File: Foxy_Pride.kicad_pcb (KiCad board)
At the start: 2 copper layers, 89.3 x 67.9 mm, 36 parts, among them U1 TLC555CDR, U2 74HC4017D

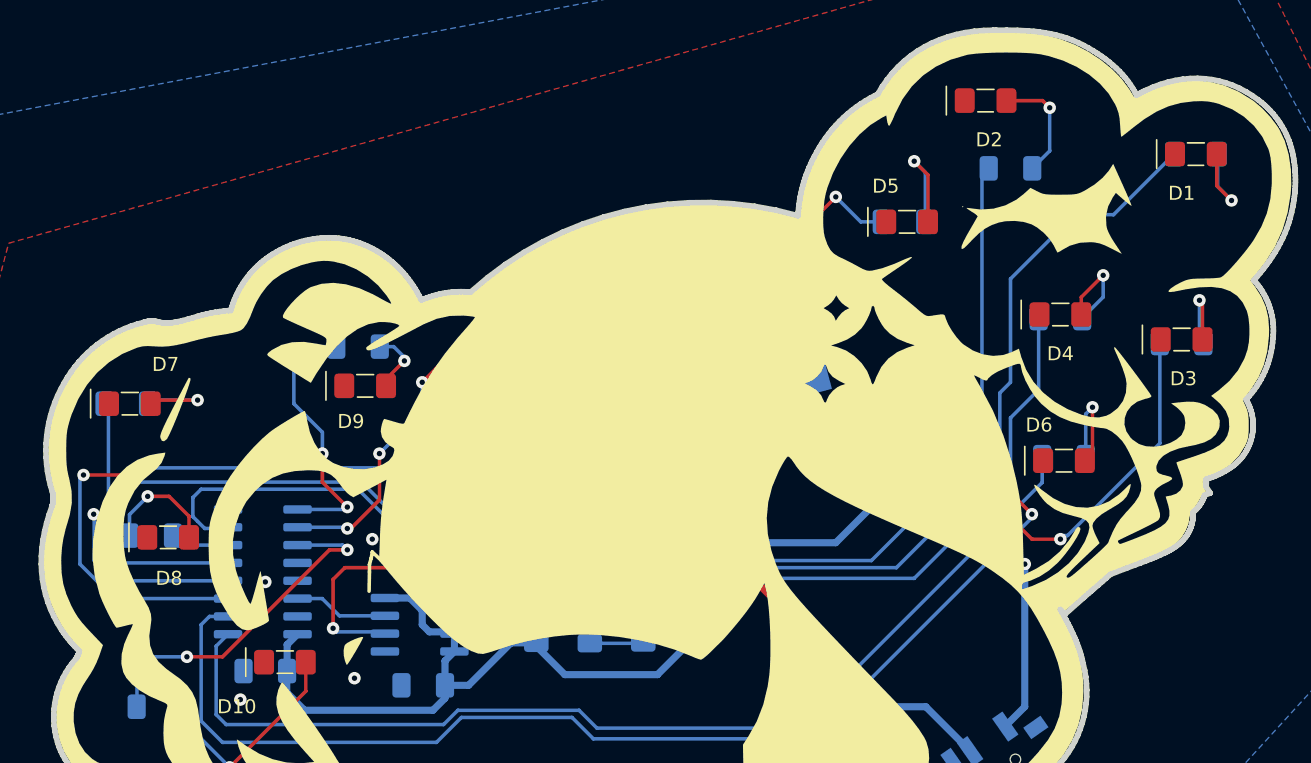
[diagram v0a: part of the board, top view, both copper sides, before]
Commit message: Re annontated schematic so resistors and LEDs have matching refrence designators
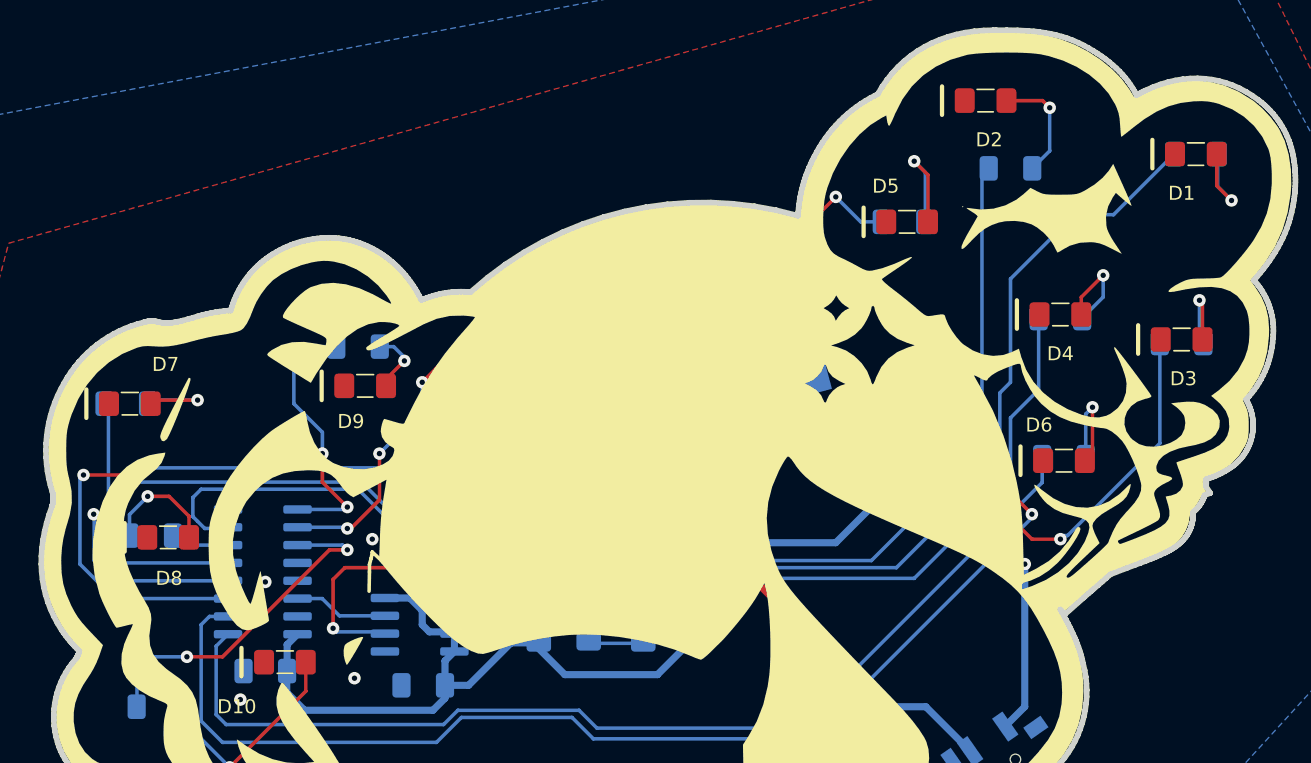
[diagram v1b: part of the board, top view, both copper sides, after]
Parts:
- removed the R1 at (61.7, 76.7)
- removed the R2 at (65.5, 76.7)
- added R11: 10M, Resistor_SMD:R_1206_3216Metric_Pad1.30x1.75mm_HandSolder, B.Cu at (61.9, 76.7)
- added R12: 2.2M, Resistor_SMD:R_1206_3216Metric_Pad1.30x1.75mm_HandSolder, B.Cu at (65.5, 76.6)
- moved G*** 2.06 mm to (85.8, 74.0)
- renumbered R3 to R1, R12 to R10, R4 to R2, R5 to R3, R6 to R4, R7 to R5, R8 to R6, R9 to R7, R10 to R8, R11 to R9
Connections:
- net +Vbatt renamed <NO NET>
- S1 pad : GND -> (no net)

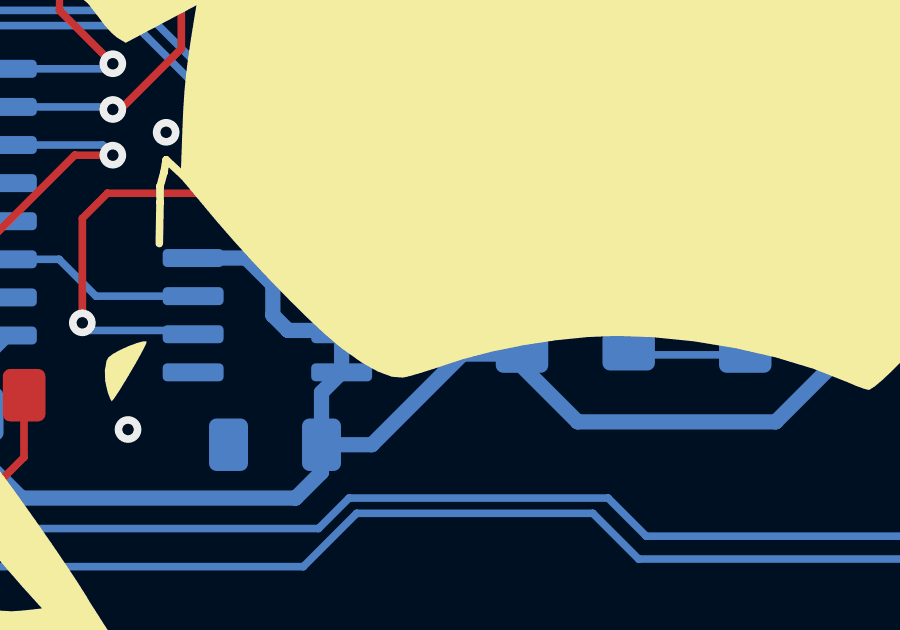
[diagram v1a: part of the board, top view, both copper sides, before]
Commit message: Changed schematic layout. Put resistor in correct spot. Update PCB.
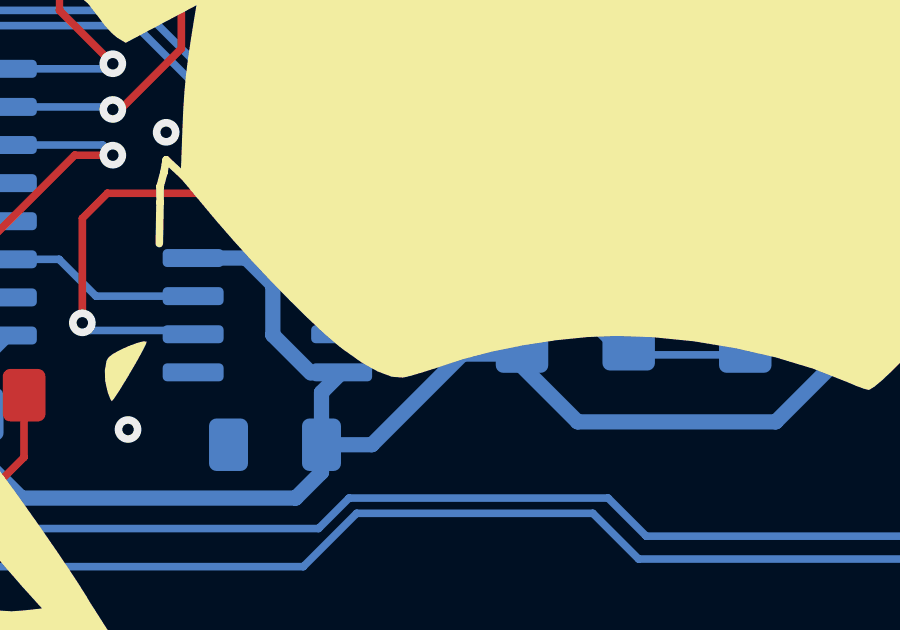
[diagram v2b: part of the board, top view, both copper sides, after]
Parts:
- renumbered G*** to ?
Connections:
- R11 pad 2: Net-(U1-Pad2) -> Net-(R11-Pad2)
- R12 pad 1: Net-(U1-Pad2) -> Net-(R11-Pad2)
- U1 pad 2: Net-(U1-Pad2) -> Net-(C1-Pad1)
- U1 pad 6: Net-(U1-Pad2) -> Net-(C1-Pad1)
- U1 pad 7: +3V -> Net-(R11-Pad2)
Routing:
- net Net-(C1-Pad1): track 3.83 -> 35.1 mm, vias 0 -> 4
- net Net-(U1-Pad2): track 30.2 -> 0.00 mm, vias 2 -> 0
- net Net-(R11-Pad2): track 0.00 -> 10.6 mm
- net +3V: track 77.0 -> 75.7 mm

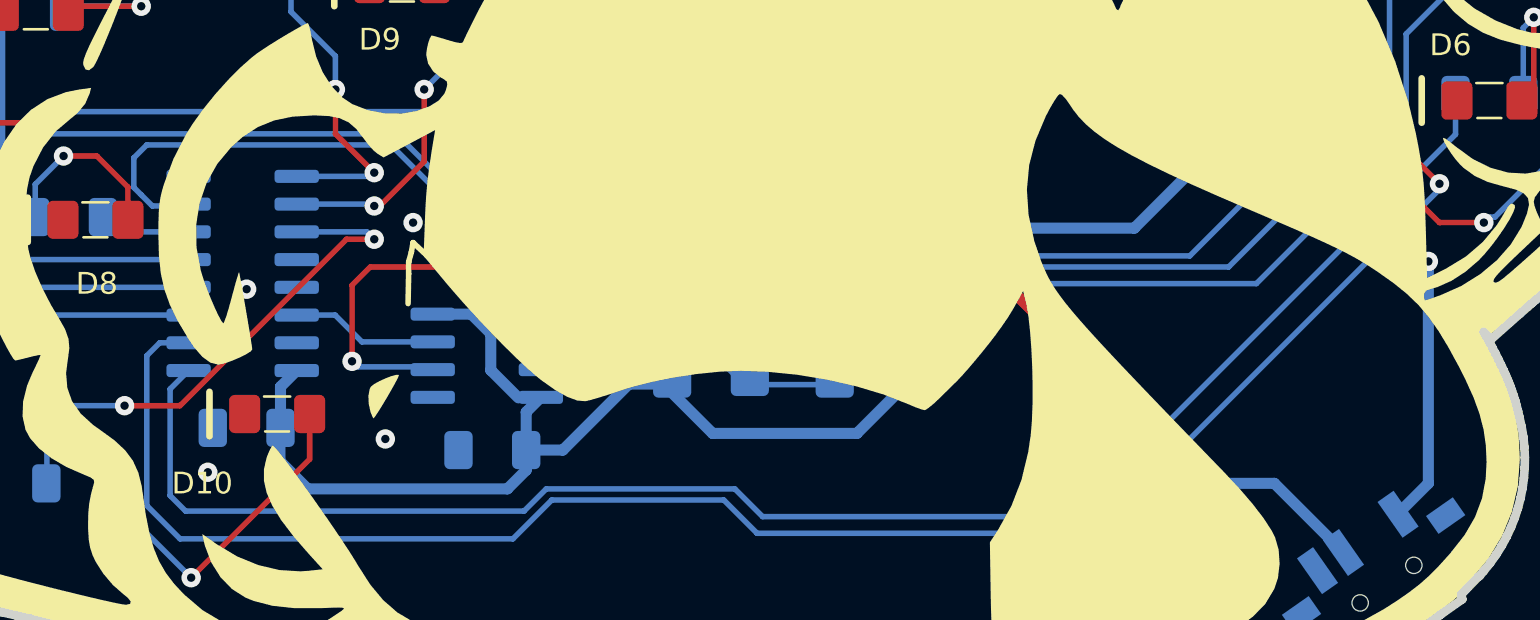
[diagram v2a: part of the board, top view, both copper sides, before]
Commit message: Repositioned resistor and capacitor
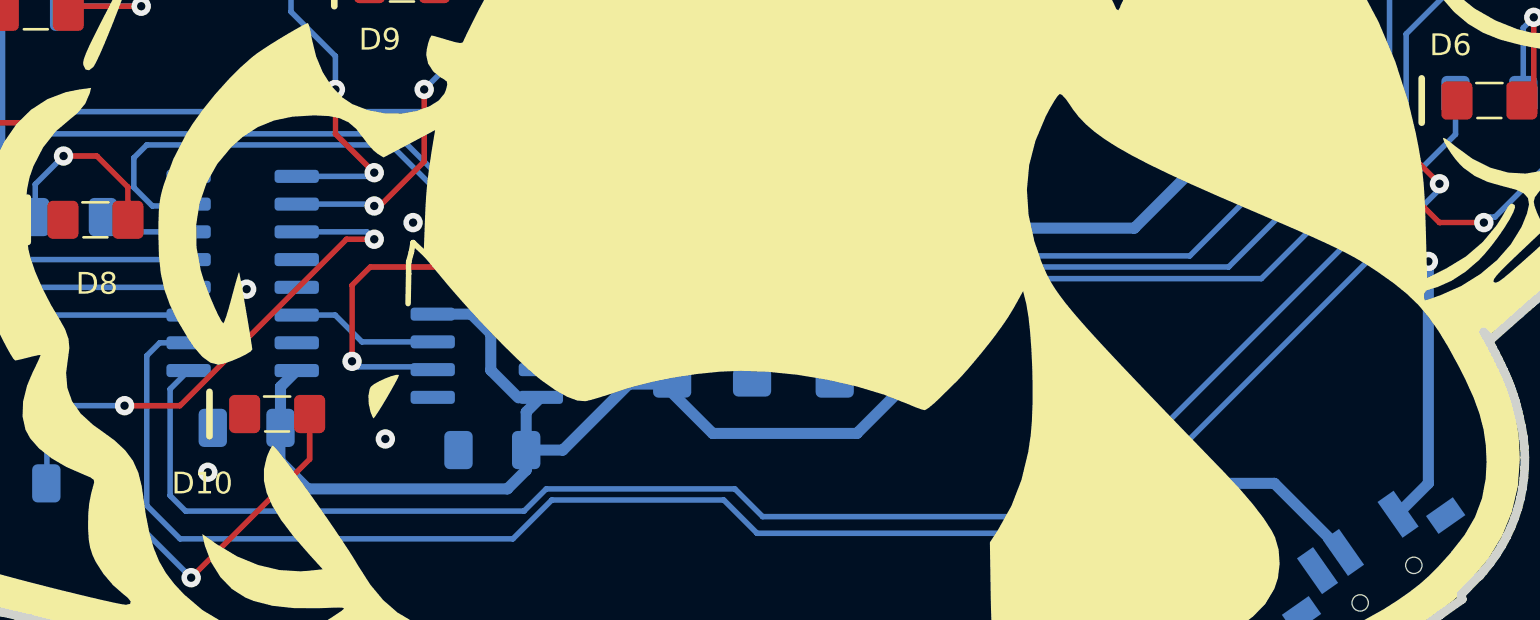
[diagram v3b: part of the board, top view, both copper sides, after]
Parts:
- moved R12 0.10 mm to (65.6, 76.6), turned to 90 degrees
- turned C1 to -90 degrees
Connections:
- net <NO NET> renamed +Vbatt
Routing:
- net Net-(R11-Pad2): track 10.6 -> 12.0 mm
- net +3V: track 75.7 -> 75.1 mm
- net Net-(C1-Pad1): track 35.1 -> 34.8 mm, vias 4 -> 2

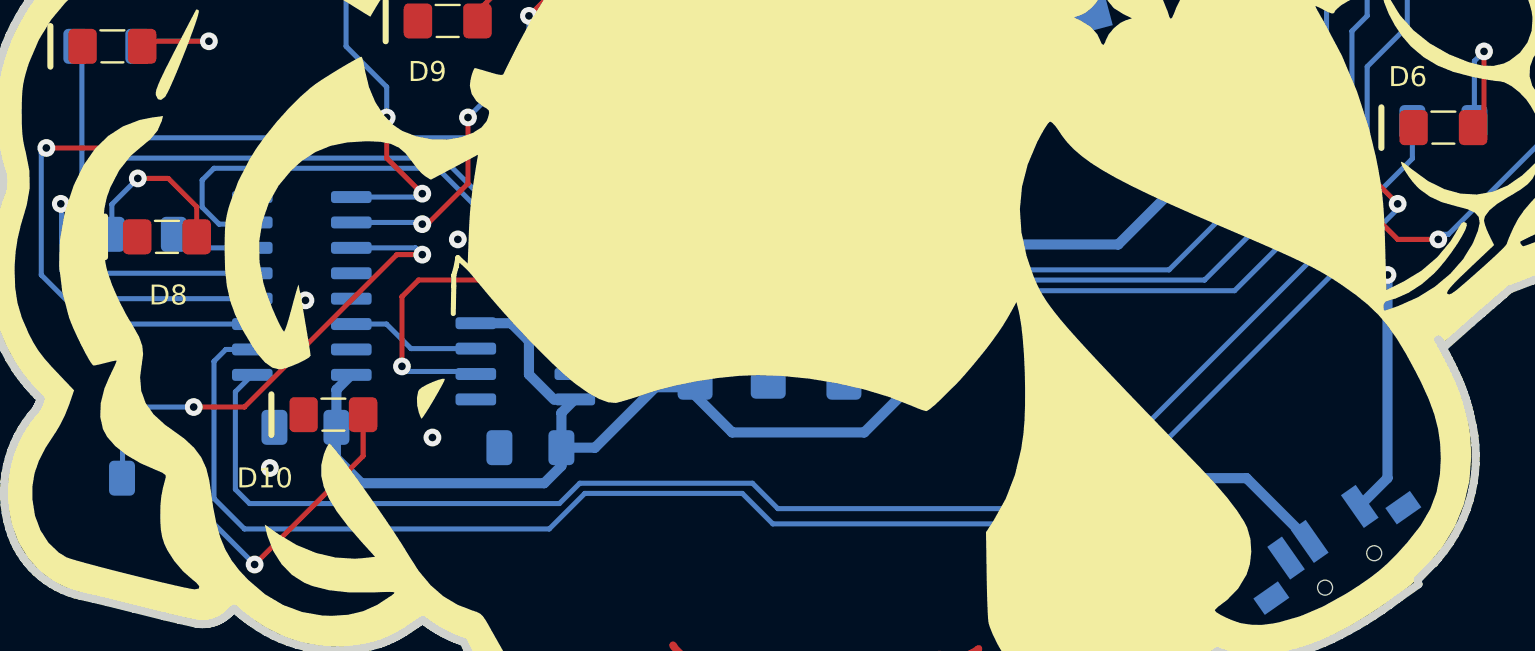
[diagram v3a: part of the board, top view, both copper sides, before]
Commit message: Update 555 timer footprint and decasde counter. had to fix a couple tranes after.
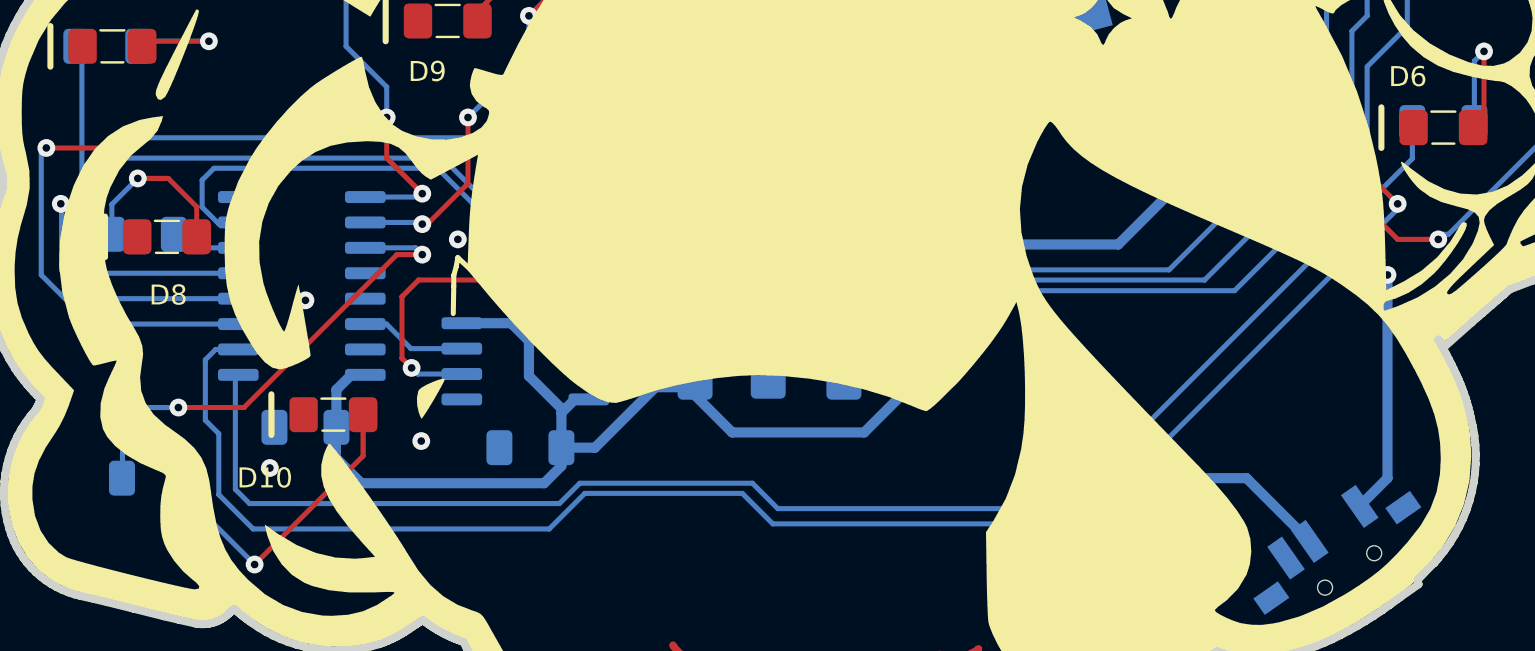
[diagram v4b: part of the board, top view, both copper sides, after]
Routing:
- net +3V: track 75.1 -> 75.8 mm

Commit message: Updated Final Design
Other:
- board text added: "@AlpenglowInd"
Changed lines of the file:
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@@
     (fp_circle (center -4.445 5.588) (end -4.191 5.588) (layer "B.SilkS") (width 0.12) (fill solid))
     (fp_line (start 3.7 -5.2) (end 3.7 5.2) (layer "B.CrtYd") (width 0.05))
+    (fp_line (start -3.7 -5.2) (end 3.7 -5.2) (layer "B.CrtYd") (width 0.05))
     (fp_line (start -3.7 5.2) (end -3.7 -5.2) (layer "B.CrtYd") (width 0.05))
-    (fp_line (start -3.7 -5.2) (end 3.7 -5.2) (layer "B.CrtYd") (width 0.05))
     (fp_line (start 3.7 5.2) (end -3.7 5.2) (layer "B.CrtYd") (width 0.05))
+    (fp_line (start -1.95 3.975) (end -0.975 4.95) (layer "B.Fab") (width 0.1))
     (fp_line (start -1.95 -4.95) (end -1.95 3.975) (layer "B.Fab") (width 0.1))
+    (fp_line (start 1.95 -4.95) (end -1.95 -4.95) (layer "B.Fab") (width 0.1))
+    (fp_line (start -0.975 4.95) (end 1.95 4.95) (layer "B.Fab") (width 0.1))
     (fp_line (start 1.95 4.95) (end 1.95 -4.95) (layer "B.Fab") (width 0.1))
-    (fp_line (start -0.975 4.95) (end 1.95 4.95) (layer "B.Fab") (width 0.1))
-    (fp_line (start 1.95 -4.95) (end -1.95 -4.95) (layer "B.Fab") (width 0.1))
-    (fp_line (start -1.95 3.975) (end -0.975 4.95) (layer "B.Fab") (width 0.1))
     (pad "1" smd roundrect (at -3.175 4.445) (size 2.032 0.6) (layers "B.Cu" "B.Paste" "B.Mask") (roundrect_rratio 0.25)
       (net 24 "Net-(R6-Pad2)") (pinfunction "Q5") (pintype "output"))
@@
     (effects (font (size 1.524 1.524) (thickness 0.2286)) (justify mirror))
   )
+  (gr_text "@AlpenglowInd" (at 79.4512 84.6074) (layer "B.SilkS")
+    (effects (font (size 1.27 1.397) (thickness 0.1778)) (justify mirror))
+  )
   (via (at 73.152 63.754) (size 0.889) (drill 0.381) (layers "F.Cu" "B.Cu") (free) (net 1))

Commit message: Updated board name with font, updated @alpenglowind with font
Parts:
- added G***: LOGO, FoxyPride:FXP board name font 20x3.3mm, B.Cu at (84.5, 79.0)
- added G***: LOGO, Alpenglow:@AlpenglowIndOswald20mm, B.Cu at (86.2, 77.8)
- moved ? 4.49 mm to (87.5, 69.8)
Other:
- board text removed: "@AlpenglowInd"
- board text removed: "Foxy Pride"
